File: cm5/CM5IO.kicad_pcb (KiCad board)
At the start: 4 copper layers, 101.9 x 90.8 mm, 67 parts, among them J1 67910-5700, J14 JST_SHBM04B-SRSS-TB, J2 1x4, J4 0786463001, J5 USB3_A, J6 Conn_02x03_Counter_Clockwise, J7 Conn_01x04, U2 TLV320ADC6120IRTER, U5 74LVC1G07SE-7, U6 AP22653W6, U8 AP3441SHE-7B

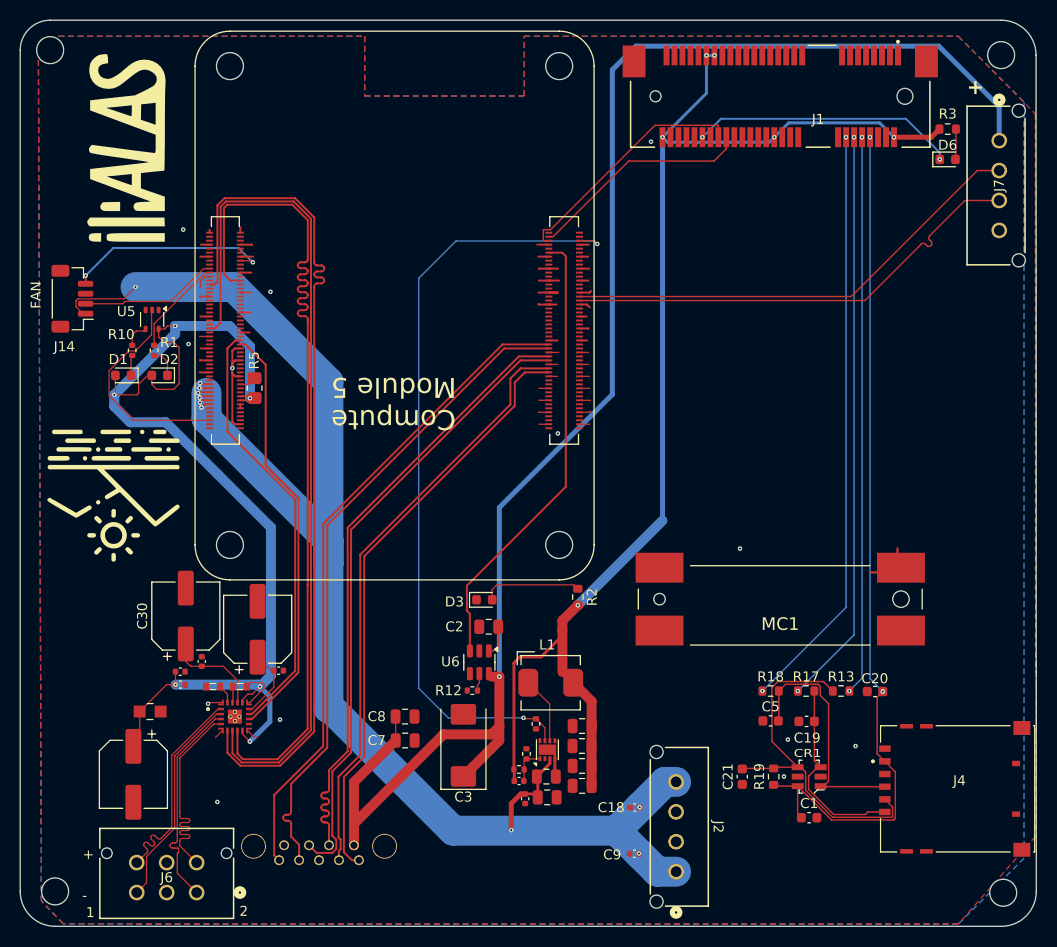
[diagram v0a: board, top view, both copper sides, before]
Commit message: PCM1863 switchover (#5)
* Oops, basically brand new ADC design using a new chip

* Working PCB and working driver, sort of

* --amend
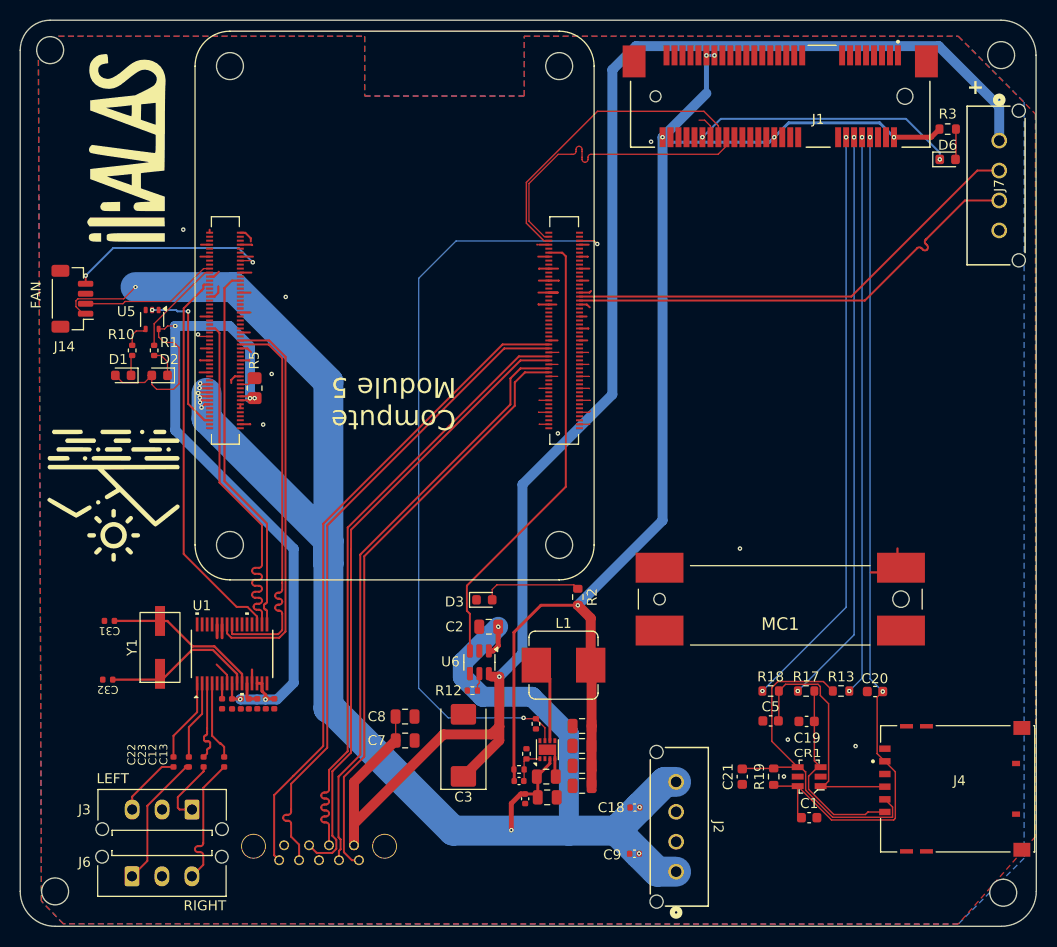
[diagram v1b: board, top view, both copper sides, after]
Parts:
- removed U2: TLV320ADC6120IRTER, TLV320ADC6120IRTER:IC_TLV320ADC6120IRTER
- added C22: 10uF, PCM_JLCPCB:C_0402, F.Cu at (156.8, 143.2)
- added C23: 10uF, PCM_JLCPCB:C_0402, F.Cu at (158.4, 143.2)
- added C32: 15pF, PCM_JLCPCB:C_0402, F.Cu at (150.2, 135.0)
- added J3: Conn_01x03, Connector_Molex:Molex_Micro-Fit_3.0_43650-0315_1x03_P3.00mm_Vertical, F.Cu at (158.7, 148.0)
- added U1: PCM1863DBT, PCM:DBT30_TEX, F.Cu at (162.7, 132.4)
- added Y1: Crystal (24.576MHz), Crystal:S47SMD, F.Cu at (155.5, 131.8)
- C12, C13: value 1uF -> 10uF; footprint digikey-footprints:0603 -> PCM_JLCPCB:C_0402
- C24: footprint digikey-footprints:0805 -> PCM_JLCPCB:C_0402
- C25, C29: value 100n -> 10uF; footprint Capacitor_SMD:C_0402_1005Metric -> PCM_JLCPCB:C_0402
- C26: value 100n -> 100nF; footprint Capacitor_SMD:C_0402_1005Metric -> PCM_JLCPCB:C_0402
- C27: footprint Capacitor_SMD:CP_Elec_6.3x5.9 -> PCM_JLCPCB:C_0402
- C28, C30: value 10uF -> 100nF; footprint Capacitor_SMD:CP_Elec_6.3x5.9 -> PCM_JLCPCB:C_0402
- C31: value 100n -> 15pF; footprint Capacitor_SMD:C_0402_1005Metric -> PCM_JLCPCB:C_0402
- J6: value Conn_02x03_Counter_Clockwise -> Conn_01x03; footprint Connector_Molex:CONN_SD-43045-005_06_MOL 2x3 -> Connector_Molex:Molex_Micro-Fit_3.0_43650-0315_1x03_P3.00mm_Vertical
- L1: footprint CM5IO:L_Bourns_SRP5030CC -> Inductor_SMD:L_Bourns_SRP7028A_7.3x6.6mm
- moved C27 15.8 mm to (166.9, 137.4), turned to 90 degrees
- moved C30 11.3 mm to (165.2, 137.4), turned to -90 degrees
- moved C31 10.1 mm to (150.4, 129.1), turned to 180 degrees
- moved C13 7.71 mm to (161.9, 143.2), turned to 90 degrees
- moved C12 7.61 mm to (159.9, 143.2), turned to 90 degrees
- moved C28 7.51 mm to (166.1, 137.4), turned to -90 degrees
- moved C24 7.25 mm to (161.7, 137.4), turned to 90 degrees
- moved J6 6.68 mm to (152.7, 154.7)
- moved C25 6.37 mm to (163.6, 137.4), turned to 90 degrees
- moved C26 6.11 mm to (162.7, 137.4), turned to 90 degrees
- moved C29 4.48 mm to (164.4, 137.4), turned to 90 degrees
- moved L1 2.18 mm to (195.9, 133.6)
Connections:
- net /PCIe-M2/DTR renamed /Cellular/DTR
- net /PCIe-M2/FB renamed /Cellular/FB
- net /PCIe-M2/LED_WWAN renamed /Cellular/LED_WWAN
- net /PCIe-M2/M2_3v3 renamed /Cellular/M2_3v3
- net /PCIe-M2/PERST renamed /Cellular/PERST
- net /PCIe-M2/RI renamed /Cellular/RI
- net /PCIe-M2/SIM_CLK renamed /Cellular/SIM_CLK
- net /PCIe-M2/SIM_DATA renamed /Cellular/SIM_DATA
- net /PCIe-M2/SIM_RST renamed /Cellular/SIM_RST
- net /PCIe-M2/SIM_VDD renamed /Cellular/SIM_VDD
- net /PCIe-M2/W_DISABLE renamed /Cellular/W_DISABLE
- C12 pad 1: Net-(U2-MICBIAS_GPI2) -> /CM5_GPIO ( Ethernet, GPIO, SDCARD)/Audio/LP
- C12 pad 2: GND -> /CM5_GPIO ( Ethernet, GPIO, SDCARD)/Audio/VIN1P
- C13 pad 1: Net-(U2-VREF) -> /CM5_GPIO ( Ethernet, GPIO, SDCARD)/Audio/RP
- C13 pad 2: GND -> /CM5_GPIO ( Ethernet, GPIO, SDCARD)/Audio/VIN2P
- C2 pad 1: /CM5_HighSpeed/+5v -> /+5v
- C24 pad 1: /+3.3v -> GND
- C24 pad 2: GND -> Net-(U1-VREF)
- C25 pad 1: /+3.3v -> GND
- C25 pad 2: GND -> /+3.3v
- C26 pad 1: /+3.3v -> GND
- C26 pad 2: GND -> /+3.3v
- C27 pad 1: /+3.3v -> GND
- C27 pad 2: GND -> /+3.3v
- C28 pad 1: /CM5_GPIO ( Ethernet, GPIO, SDCARD)/DREG -> /+3.3v
- C29 pad 1: /CM5_GPIO ( Ethernet, GPIO, SDCARD)/DREG -> GND
- C29 pad 2: GND -> /CM5_GPIO ( Ethernet, GPIO, SDCARD)/Audio/LDO
- C30 pad 1: /CM5_GPIO ( Ethernet, GPIO, SDCARD)/AREG -> /CM5_GPIO ( Ethernet, GPIO, SDCARD)/Audio/LDO
- C31 pad 1: /CM5_GPIO ( Ethernet, GPIO, SDCARD)/AREG -> /CM5_GPIO ( Ethernet, GPIO, SDCARD)/Audio/XI
- J6 pad 1: Net-(J6-Pin_1) -> /CM5_GPIO ( Ethernet, GPIO, SDCARD)/Audio/RN
- J6 pad 3: Net-(J6-Pin_3) -> /CM5_GPIO ( Ethernet, GPIO, SDCARD)/Audio/RP
- Module1 pad 89: /CM5_GPIO ( Ethernet, GPIO, SDCARD)/WL_nDis -> unconnected-(Module1A-WiFi_nDisable-Pad89)
- Module1 pad 91: /CM5_GPIO ( Ethernet, GPIO, SDCARD)/BT_nDis -> unconnected-(Module1A-BT_nDisable-Pad91)
- Module1 pad 97: /CM5_GPIO ( Ethernet, GPIO, SDCARD)/CAM_GPIO0 -> unconnected-(Module1A-CAM_GPIO0-Pad97)
- U6 pad 1: /CM5_HighSpeed/+5v -> /+5v
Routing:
- net /CM5_GPIO ( Ethernet, GPIO, SDCARD)/GPIO19: track 86.7 -> 37.7 mm
- net /CM5_GPIO ( Ethernet, GPIO, SDCARD)/GPIO18: track 86.1 -> 37.5 mm
- net /CM5_GPIO ( Ethernet, GPIO, SDCARD)/GPIO20: track 86.7 -> 39.1 mm
- net /+5v: track 152.8 -> 185.1 mm, vias 10 -> 11
- net /+3.3v: track 113.1 -> 86.0 mm, vias 6 -> 5
- net Net-(J6-Pin_3): track 21.6 -> 0.00 mm
- net Net-(J6-Pin_1): track 21.6 -> 0.00 mm
- net Net-(J6-Pin_6): track 21.6 -> 0.00 mm
- net Net-(J6-Pin_4): track 21.5 -> 0.00 mm
- net /CM5_GPIO ( Ethernet, GPIO, SDCARD)/Audio/XI: track 0.00 -> 15.9 mm
- net /CM5_GPIO ( Ethernet, GPIO, SDCARD)/Audio/XO: track 0.00 -> 15.8 mm
- net /CM5_GPIO ( Ethernet, GPIO, SDCARD)/Audio/RN: track 0.00 -> 13.5 mm
- net /CM5_GPIO ( Ethernet, GPIO, SDCARD)/Audio/RP: track 0.00 -> 13.4 mm
- net /CM5_GPIO ( Ethernet, GPIO, SDCARD)/AREG: track 9.92 -> 0.00 mm
- net /CM5_HighSpeed/USB2_N: track 22.6 -> 31.0 mm
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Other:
- board text added: "LEFT"
- board text added: "RIGHT"
- board text removed: "-"
- board text removed: "1"
- board text removed: "2"
